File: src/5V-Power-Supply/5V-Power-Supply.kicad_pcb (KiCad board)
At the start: 2 copper layers, 18 parts, among them P1 0901471110, P2 0901471110, U1 LM22672MRE-5.0_NOPB

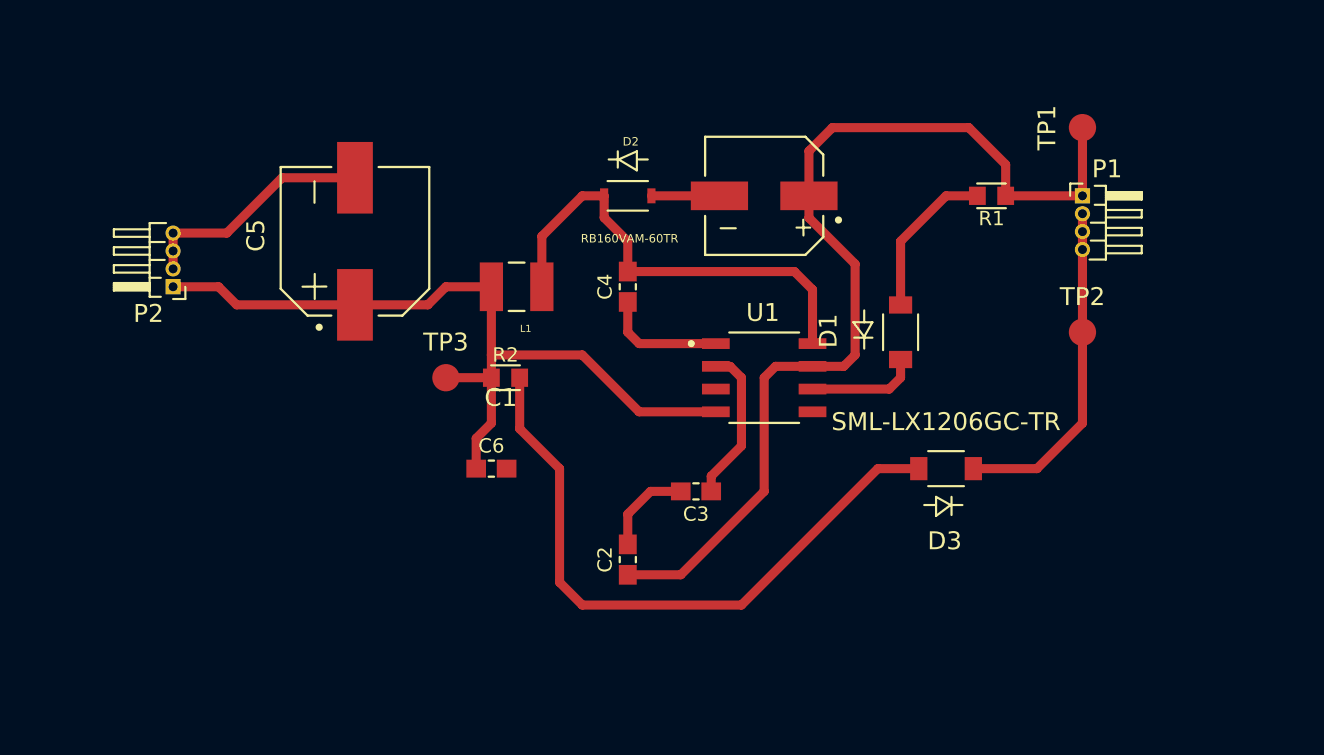
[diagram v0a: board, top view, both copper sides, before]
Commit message: added back copper filled ground
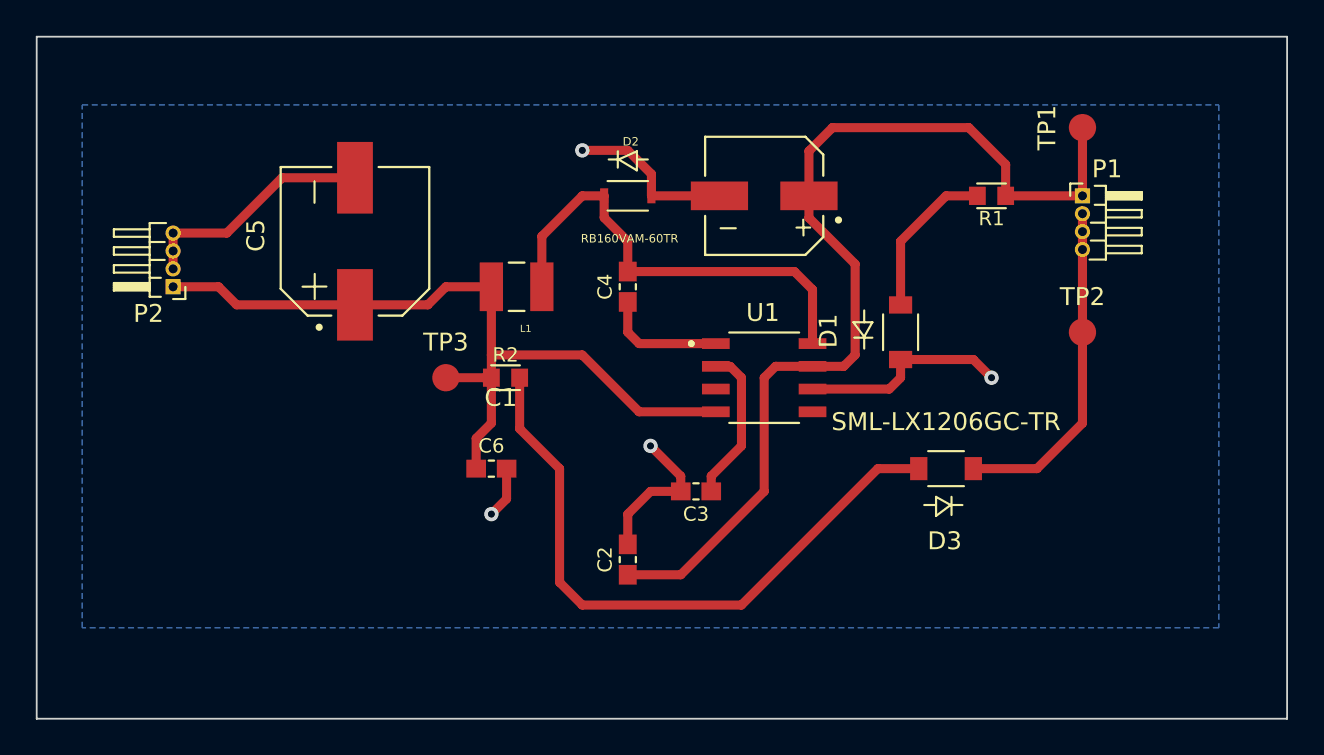
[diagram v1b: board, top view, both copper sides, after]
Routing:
- net Earth: track 47.5 -> 64.7 mm, vias 0 -> 4
- added copper zone on B.Cu, net Earth
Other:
- board outline added: 69.9 x 38.1 mm
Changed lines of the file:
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@@
     )
   )
+  (gr_line (start 194.31 74.93) (end 124.46 74.93) (layer "Edge.Cuts") (width 0.1))
+  (gr_line (start 124.46 113.03) (end 194.31 113.03) (layer "Edge.Cuts") (width 0.1))
+  (gr_line (start 124.46 74.93) (end 124.46 113.03) (layer "Edge.Cuts") (width 0.1))
+  (gr_line (start 194.31 113.03) (end 194.31 74.93) (layer "Edge.Cuts") (width 0.1))
   (segment (start 165.1 93.98) (end 165.1 100.33) (width 0.508) (layer "F.Cu") (net 1))
   (segment (start 182.88 80.01) (end 182.88 83.82) (width 0.508) (layer "F.Cu") (net 1))
@@
   (segment (start 165.735 93.345) (end 165.1 93.98) (width 0.508) (layer "F.Cu") (net 1))
   (segment (start 138.17 82.81) (end 142.24 82.81) (width 0.508) (layer "F.Cu") (net 2))
+  (segment (start 150.71 99.06) (end 150.71 100.75) (width 0.508) (layer "F.Cu") (net 2))
+  (segment (start 157.48 81.28) (end 154.94 81.28) (width 0.508) (layer "F.Cu") (net 2))
   (segment (start 132.08 85.9) (end 135.08 85.9) (width 0.508) (layer "F.Cu") (net 2))
   (segment (start 167.8 94.615) (end 172.085 94.615) (width 0.508) (layer "F.Cu") (net 2))
@@
   (segment (start 182.88 84.82) (end 182.88 85.82) (width 0.508) (layer "F.Cu") (net 2))
   (segment (start 158.75 100.33) (end 160.44 100.33) (width 0.508) (layer "F.Cu") (net 2))
+  (segment (start 158.8008 83.82) (end 158.8008 82.6008) (width 0.508) (layer "F.Cu") (net 2))
   (segment (start 157.48 101.6) (end 158.75 100.33) (width 0.508) (layer "F.Cu") (net 2))
   (segment (start 172.085 94.615) (end 172.72 93.98) (width 0.508) (layer "F.Cu") (net 2))
+  (segment (start 160.44 100.33) (end 160.44 99.48) (width 0.508) (layer "F.Cu") (net 2))
   (segment (start 182.88 86.82) (end 182.88 91.44) (width 0.508) (layer "F.Cu") (net 2))
   (segment (start 135.08 85.9) (end 138.17 82.81) (width 0.508) (layer "F.Cu") (net 2))
+  (segment (start 158.8008 82.6008) (end 157.48 81.28) (width 0.508) (layer "F.Cu") (net 2))
+  (segment (start 172.72 92.964) (end 176.784 92.964) (width 0.508) (layer "F.Cu") (net 2))
+  (segment (start 150.71 100.75) (end 149.86 101.6) (width 0.508) (layer "F.Cu") (net 2))
   (segment (start 180.34 99.06) (end 182.88 96.52) (width 0.508) (layer "F.Cu") (net 2))
+  (segment (start 160.44 99.48) (end 158.75 97.79) (width 0.508) (layer "F.Cu") (net 2))
   (segment (start 132.08 87.9) (end 132.08 86.9) (width 0.508) (layer "F.Cu") (net 2))
   (segment (start 182.88 96.52) (end 182.88 91.44) (width 0.508) (layer "F.Cu") (net 2))
   (segment (start 157.48 103.29) (end 157.48 101.6) (width 0.508) (layer "F.Cu") (net 2))
+  (segment (start 176.784 92.964) (end 177.8 93.98) (width 0.508) (layer "F.Cu") (net 2))
+  (via (at 149.86 101.6) (size 0.8) (drill 0.4) (layers "F.Cu" "B.Cu") (free) (net 2))
+  (via (at 154.94 81.28) (size 0.8) (drill 0.4) (layers "F.Cu" "B.Cu") (free) (net 2))
+  (via (at 158.75 97.79) (size 0.8) (drill 0.4) (layers "F.Cu" "B.Cu") (free) (net 2))
+  (via (at 177.8 93.98) (size 0.8) (drill 0.4) (layers "F.Cu" "B.Cu") (free) (net 2))
   (segment (start 162.14 99.48) (end 162.14 100.33) (width 0.508) (layer "F.Cu") (net 3))
   (segment (start 163.83 97.79) (end 162.14 99.48) (width 0.508) (layer "F.Cu") (net 3))
@@
   (segment (start 153.67 105.41) (end 154.94 106.68) (width 0.508) (layer "F.Cu") (net 8))
   (segment (start 151.44 93.98) (end 151.44 96.83) (width 0.508) (layer "F.Cu") (net 8))
+  (zone (net 2) (net_name "Earth") (layer "B.Cu") (hatch edge 0.508)
+    (connect_pads (clearance 0.508))
+    (min_thickness 0.254) (filled_areas_thickness no)
+    (fill yes (thermal_gap 0.508) (thermal_bridge_width 0.508))
+    (polygon
+      (pts
+        (xy 190.5 107.95)
+        (xy 127 107.95)
+        (xy 127 78.74)
+        (xy 190.5 78.74)
+      )
+    )
+  )
 )
